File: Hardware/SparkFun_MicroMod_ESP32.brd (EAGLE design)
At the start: 22 x 22 mm, 53 parts, among them J1 MICROMOD-2222, Q2 MBT3904DW1T1, U1 W25QXX128MBIT-6X5, U2 ESP3212, U4 CP2102N, Y1 40MHZ, Y2 32.768kHz

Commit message: updated Prod_IDs
Added missing PROD_IDs
Added Logos to sch
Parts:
- C18: value 100PF -> 100pF
- LOGO2: value (none) -> SFE_LOGO_NAME_FLAME.1_INCH
- LOGO3: value (none) -> OSHW-LOGOS
- R4: value 47.5k -> 33k
- renumbered U$5 to LOGO2, U$8 to LOGO3
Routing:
- net GND: vias 43 -> 46

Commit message: Update SparkFun_MicroMod_ESP32.brd
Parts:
- moved L2 0.25 mm to (1.40, 13.8)
- moved L1 0.25 mm to (2.81, 12.8)
- moved C10 0.13 mm to (1.40, 11.8)
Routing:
- net N$6: track 1.83 -> 2.44 mm
- net GND: vias 46 -> 45
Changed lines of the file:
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@@
 <?xml version="1.0" encoding="utf-8"?>
 <!DOCTYPE eagle SYSTEM "eagle.dtd">
-<eagle version="9.4.1">
+<eagle version="9.6.0">
 <drawing>
 <settings>
@@
 <setting verticaltext="up"/>
 </settings>
-<grid distance="0.05" unitdist="inch" unit="mm" style="lines" multiple="1" display="yes" altdistance="0.005" altunitdist="inch" altunit="inch"/>
+<grid distance="0.05" unitdist="inch" unit="inch" style="lines" multiple="1" display="yes" altdistance="0.005" altunitdist="inch" altunit="inch"/>
 <layers>
 <layer number="1" name="Top" color="4" fill="1" visible="yes" active="yes"/>
@@
 <layer number="38" name="bTest" color="7" fill="1" visible="no" active="yes"/>
 <layer number="39" name="tKeepout" color="4" fill="11" visible="yes" active="yes"/>
-<layer number="40" name="bKeepout" color="1" fill="11" visible="yes" active="yes"/>
+<layer number="40" name="bKeepout" color="1" fill="11" visible="no" active="yes"/>
 <layer number="41" name="tRestrict" color="4" fill="10" visible="no" active="yes"/>
 <layer number="42" name="bRestrict" color="1" fill="10" visible="no" active="yes"/>
 <layer number="43" name="vRestrict" color="2" fill="10" visible="no" active="yes"/>
 <layer number="44" name="Drills" color="7" fill="1" visible="no" active="yes"/>
-<layer number="45" name="Holes" color="7" fill="1" visible="no" active="yes"/>
+<layer number="45" name="Holes" color="7" fill="1" visible="yes" active="yes"/>
 <layer number="46" name="Milling" color="3" fill="1" visible="no" active="yes"/>
 <layer number="47" name="Measures" color="7" fill="1" visible="no" active="yes"/>
@@
 <layer number="50" name="dxf" color="7" fill="1" visible="no" active="yes"/>
 <layer number="51" name="tDocu" color="6" fill="1" visible="yes" active="yes"/>
-<layer number="52" name="bDocu" color="7" fill="1" visible="yes" active="yes"/>
+<layer number="52" name="bDocu" color="7" fill="1" visible="no" active="yes"/>
 <layer number="91" name="Nets" color="2" fill="1" visible="no" active="no"/>
 <layer number="92" name="Busses" color="1" fill="1" visible="no" active="no"/>
@@
 <layer number="95" name="Names" color="7" fill="1" visible="no" active="no"/>
 <layer number="96" name="Values" color="7" fill="1" visible="no" active="no"/>
-<layer number="2" name="Horz/PWR" color="16" fill="1" visible="yes" active="yes"/>
+<layer number="2" name="Horz/PWR" color="16" fill="1" visible="no" active="yes"/>
 <layer number="3" name="Route3" color="17" fill="1" visible="no" active="no"/>
 <layer number="4" name="Route4" color="18" fill="1" visible="no" active="no"/>
@@
 <layer number="13" name="Route13" color="21" fill="1" visible="no" active="no"/>
 <layer number="14" name="Route14" color="22" fill="1" visible="no" active="no"/>
-<layer number="15" name="VIRT/GND" color="23" fill="1" visible="yes" active="yes"/>
+<layer number="15" name="VIRT/GND" color="23" fill="1" visible="no" active="yes"/>
 <layer number="53" name="tGND_GNDA" color="7" fill="9" visible="no" active="no"/>
 <layer number="54" name="bGND_GNDA" color="1" fill="9" visible="no" active="no"/>
@@
 <attribute name="VALUE" x="7.781" y="11.137" size="0.762" layer="28" rot="MR90" align="center"/>
 </element>
-<element name="L1" library="SparkFun-Coils" package="0402-TIGHT" value="2.7nH" x="2.812" y="13.08" smashed="yes">
-<attribute name="NAME" x="2.812" y="13.642" size="0.6096" layer="25" font="vector" ratio="20" align="bottom-center"/>
-<attribute name="PROD_ID" value="NDUC-14236" x="2.812" y="13.08" size="1.778" layer="27" font="vector" ratio="15" display="off"/>
-<attribute name="VALUE" x="2.812" y="12.518" size="0.6096" layer="27" font="vector" ratio="20" align="top-center"/>
-</element>
-<element name="L2" library="SparkFun-Coils" package="0402-TIGHT" value="2nH" x="1.397" y="13.578" smashed="yes" rot="R270">
-<attribute name="NAME" x="1.959" y="13.578" size="0.6096" layer="25" font="vector" ratio="20" rot="R270" align="bottom-center"/>
-<attribute name="PROD_ID" value="NDUC-14238" x="1.397" y="13.578" size="1.778" layer="27" font="vector" ratio="15" rot="R270" display="off"/>
-<attribute name="VALUE" x="0.835" y="13.578" size="0.6096" layer="27" font="vector" ratio="20" rot="R270" align="top-center"/>
-</element>
-<element name="C10" library="SparkFun-Capacitors" package="0402-TIGHT" value="0.5pF" x="1.397" y="11.667" smashed="yes" rot="R270">
-<attribute name="NAME" x="1.959" y="11.667" size="0.6096" layer="25" font="vector" ratio="20" rot="R270" align="bottom-center"/>
-<attribute name="PROD_ID" value="CAP-14362" x="1.397" y="11.667" size="1.778" layer="27" font="vector" ratio="15" rot="R270" display="off"/>
-<attribute name="VALUE" x="0.835" y="11.667" size="0.6096" layer="27" font="vector" ratio="20" rot="R270" align="top-center"/>
+<element name="L1" library="SparkFun-Coils" package="0402-TIGHT" value="2.7nH" x="2.812" y="12.826" smashed="yes">
+<attribute name="NAME" x="2.812" y="13.388" size="0.6096" layer="25" font="vector" ratio="20" align="bottom-center"/>
+<attribute name="PROD_ID" value="NDUC-14236" x="2.812" y="12.826" size="1.778" layer="27" font="vector" ratio="15" display="off"/>
+<attribute name="VALUE" x="2.812" y="12.264" size="0.6096" layer="27" font="vector" ratio="20" align="top-center"/>
+</element>
+<element name="L2" library="SparkFun-Coils" package="0402-TIGHT" value="2nH" x="1.397" y="13.832" smashed="yes" rot="R270">
+<attribute name="NAME" x="1.959" y="13.832" size="0.6096" layer="25" font="vector" ratio="20" rot="R270" align="bottom-center"/>
+<attribute name="PROD_ID" value="NDUC-14238" x="1.397" y="13.832" size="1.778" layer="27" font="vector" ratio="15" rot="R270" display="off"/>
+<attribute name="VALUE" x="0.835" y="13.832" size="0.6096" layer="27" font="vector" ratio="20" rot="R270" align="top-center"/>
+</element>
+<element name="C10" library="SparkFun-Capacitors" package="0402-TIGHT" value="0.5pF" x="1.397" y="11.794" smashed="yes" rot="R270">
+<attribute name="NAME" x="1.959" y="11.794" size="0.6096" layer="25" font="vector" ratio="20" rot="R270" align="bottom-center"/>
+<attribute name="PROD_ID" value="CAP-14362" x="1.397" y="11.794" size="1.778" layer="27" font="vector" ratio="15" rot="R270" display="off"/>
+<attribute name="VALUE" x="0.835" y="11.794" size="0.6096" layer="27" font="vector" ratio="20" rot="R270" align="top-center"/>
 </element>
 <element name="FD1" library="SparkFun-Aesthetics" package="FIDUCIAL-MICRO" value="FIDUCIALUFIDUCIAL" x="0.614" y="5" smashed="yes"/>
@@
 <via x="5.978" y="13.751" extent="1-16" drill="0.2"/>
 <via x="7.108" y="13.471" extent="1-16" drill="0.2"/>
-<via x="2.818" y="12.391" extent="1-16" drill="0.2"/>
+<via x="2.818" y="12.137" extent="1-16" drill="0.2"/>
 <via x="1.088" y="6.011" extent="1-16" drill="0.2"/>
-<via x="6.378" y="12.551" extent="1-16" drill="0.2"/>
 <wire x1="9.15" y1="17.718" x2="8.93" y2="17.498" width="0.2032" layer="1"/>
 <wire x1="8.93" y1="17.498" x2="7.74" y2="17.498" width="0.2032" layer="1"/>
@@
 <via x="3.988" y="13.741" extent="1-16" drill="0.2"/>
 <via x="5.008" y="13.691" extent="1-16" drill="0.2"/>
-<via x="5.588" y="12.551" extent="1-16" drill="0.2"/>
-<via x="4.768" y="12.541" extent="1-16" drill="0.2"/>
-<via x="3.948" y="12.541" extent="1-16" drill="0.2"/>
+<via x="5.969" y="12.297" extent="1-16" drill="0.2"/>
+<via x="5.022" y="12.287" extent="1-16" drill="0.2"/>
+<via x="4.075" y="12.287" extent="1-16" drill="0.2"/>
 <via x="19.62" y="15.33" extent="1-16" drill="0.2"/>
 <via x="12.972" y="18.357" extent="1-16" drill="0.2"/>
@@
 <contactref element="L2" pad="1"/>
 <contactref element="A1" pad="FEED"/>
-<wire x1="1.397" y1="14.078" x2="1.397" y2="16.08" width="0.2032" layer="1"/>
+<wire x1="1.397" y1="14.332" x2="1.397" y2="16.08" width="0.2032" layer="1"/>
 </signal>
 <signal name="N$6">
@@
 <contactref element="L1" pad="1"/>
 <contactref element="C10" pad="1"/>
-<wire x1="2.312" y1="13.08" x2="2.31" y2="13.078" width="0.2032" layer="1"/>
-<wire x1="2.31" y1="13.078" x2="1.397" y2="13.078" width="0.2032" layer="1"/>
-<wire x1="1.397" y1="12.167" x2="1.397" y2="13.078" width="0.2032" layer="1"/>
+<wire x1="2.312" y1="12.826" x2="1.423" y2="12.826" width="0.2032" layer="1"/>
+<wire x1="1.423" y1="12.826" x2="1.397" y2="12.852" width="0.2032" layer="1"/>
+<wire x1="1.397" y1="13.332" x2="1.397" y2="12.852" width="0.2032" layer="1"/>
+<wire x1="1.397" y1="12.294" x2="1.397" y2="13.332" width="0.2032" layer="1"/>
 </signal>
 <signal name="N$8">
 <contactref element="U2" pad="2"/>
 <contactref element="L1" pad="2"/>
-<wire x1="6.87" y1="12.8" x2="8.05" y2="12.8" width="0.2032" layer="1"/>
-<wire x1="3.312" y1="13.08" x2="6.59" y2="13.08" width="0.2032" layer="1"/>
-<wire x1="6.59" y1="13.08" x2="6.87" y2="12.8" width="0.2032" layer="1"/>
+<wire x1="8.05" y1="12.8" x2="3.455" y2="12.8" width="0.2032" layer="1"/>
+<wire x1="3.455" y1="12.8" x2="3.429" y2="12.826" width="0.2032" layer="1"/>
+<wire x1="3.312" y1="12.826" x2="3.429" y2="12.826" width="0.2032" layer="1"/>
 </signal>
 </signals>

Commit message: Updated design
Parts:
- removed L2: 2nH, SparkFun-Coils:0402-TIGHT
- added C8: (no value), SparkFun-Capacitors:0402-TIGHT
- added TP1, TP2: (no value), SparkFun-Connectors:PAD.03X.03
- A1: device SparkFun-RF:ANT-2.4GHZ-3.2X1.6X1.2MM-REDUCED_KEEPOUT -> SparkFun-RF:ANT-2.4GHZ-8.0X1.0MM
- C10: value 0.5pF -> (none)
- Q2: device esp32-thing-temp:SC70-6 -> SparkFun-DiscreteSemi:SC70-6
- U2: value ESP3212 -> ESP32; device esp32-thing-temp:QFN48-0.4MM -> SparkFun-RF:QFN48-0.4MM
- Y1: value 40MHZ -> 40MHz
- moved C10 5.45 mm to (6.63, 13.3), turned to 90 degrees
- moved LOGO3 4.02 mm to (18.6, 5.92)
- moved L1 2.41 mm to (5.22, 12.8)
- moved C20 2.12 mm to (4.97, 16.7), turned to 90 degrees
- moved C26 2.10 mm to (4.83, 5.84), turned to 180 degrees
- moved LOGO2 2.07 mm to (7.11, 17.3)
- moved C9 2.04 mm to (2.79, 5.84), turned to 0 degrees
- moved C7 1.99 mm to (14.3, 18.0), turned to 0 degrees
- moved U4 1.35 mm to (19.0, 15.9)
- moved U$3 1.35 mm to (19.9, 17.7)
- moved A1 1.30 mm to (1.02, 16.5)
- moved R4 1.27 mm to (20.2, 19.2)
- moved R5 1.27 mm to (18.3, 19.2)
- moved R3 1.24 mm to (20.2, 20.1)
- moved C18 1.20 mm to (7.83, 17.6)
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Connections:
- net 13 renamed 13-SPI_!CS!/SD_DATA3
- net 14 renamed 14-SPI_SCK/SD_CLK
- net 15 renamed 15-SPI_MOSI/SD_CMD
- net 2 renamed 2-SPI_MISO/SD_DATA0
- net 21 renamed 21-SDA
- net 22 renamed 22-SCL
- net 23 renamed 23-D0
- net 27 renamed 27-D1
- net 34 renamed 34-A0
- net 35 renamed 35-A1
- net 39 renamed 39-BATT/3
- net 5 renamed 5-STAT_LED
- net CHIP_PU renamed !RESET
- net FLASH_SCK renamed FLASH_SD_CLK
- net FLASH_SCS renamed FLASH_SD_CMD
- net FLASH_SDI renamed FLASH_SD_DATA1
- net FLASH_SDO renamed FLASH_SD_DATA0
- net FLASH_SHD renamed FLASH_SD_DATA2
- net FLASH_SWP renamed FLASH_SD_DATA3
- removed net 0: J1.11, J1.48, Q2.6, R9.1, U2.23
- removed net 12: J1.46, J1.68, U2.18
- removed net 16: J1.20, J1.54, J1.73, U2.25
- removed net 17: J1.22, J1.56, J1.71, U2.27
- removed net 18: J1.40, U2.35
- removed net 19: J1.16, J1.42, U2.38
- removed net 25: J1.52, J1.55, J1.69, U2.14
- removed net 26: J1.50, J1.53, J1.67, U2.15
- removed net 32K_XN: C26.2, J1.47, J1.63, U2.13, Y2.P$2
- removed net 32K_XP: C9.2, J1.32, J1.65, U2.12, Y2.P$1
- removed net 4: J1.44, J1.66, U2.24
- removed net N$6: C10.1, L1.1, L2.2
- removed net V_RTC: J1.72
- new net 0-!BOOT!/I2C_!INT: J1.11, J1.16, Q2.6, R9.1, U2.23
- new net 12-SD_DATA2/G1: J1.42, J1.68, U2.18
- new net 16-G2/RX1/AUD_IN: J1.19, J1.44, J1.54, U2.25
- new net 17-G3/TX1/AUD_OUT: J1.17, J1.46, J1.56, U2.27
- new net 18-PWM0: J1.32, U2.35
- new net 19-PWM1: J1.47, U2.38
- new net 25-G4/AUD_LRCLK/SCL1: J1.48, J1.52, J1.55, U2.14
- new net 26-G5/AUD_BCLK/SDA1: J1.50, J1.53, J1.73, U2.15
- new net 32-G6/RTC: C9.2, J1.71, U2.12, Y2.P$1
- new net 33-G7/RTC: C26.2, J1.69, U2.13, Y2.P$2
- new net 4-SD_DATA1/G0: J1.40, J1.66, U2.24
- net GND: now also C8.2
- net N$5: now also C8.1, L1.1; no longer L2.1
- net N$8: now also C10.1
- net U0RXD: now also TP1.P$1; no longer J1.19
- net U0TXD: now also TP2.P$1; no longer J1.17
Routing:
- net 17: track 40.9 -> 0.00 mm, vias 4 -> 0
- net 16: track 40.6 -> 0.00 mm, vias 4 -> 0
- net 19: track 29.9 -> 0.00 mm, vias 3 -> 0
- net 0-!BOOT!/I2C_!INT: track 0.00 -> 26.9 mm, vias 0 -> 3
- net 0: track 25.5 -> 0.00 mm, vias 2 -> 0
- net 17-G3/TX1/AUD_OUT: track 0.00 -> 25.5 mm, vias 0 -> 3
- net 32K_XP: track 25.3 -> 0.00 mm, vias 2 -> 0
- net 4: track 24.5 -> 0.00 mm, vias 2 -> 0
- net 19-PWM1: track 0.00 -> 24.0 mm, vias 0 -> 2
- net 26-G5/AUD_BCLK/SDA1: track 0.00 -> 23.0 mm, vias 0 -> 2
- net 4-SD_DATA1/G0: track 0.00 -> 22.6 mm, vias 0 -> 2
- net 26: track 21.0 -> 0.00 mm, vias 2 -> 0
- net 16-G2/RX1/AUD_IN: track 0.00 -> 21.0 mm, vias 0 -> 2
- net 12-SD_DATA2/G1: track 0.00 -> 19.4 mm, vias 0 -> 2
- net 25: track 19.0 -> 0.00 mm, vias 2 -> 0
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- added copper zone on layer 15, net 3.3V
- added copper zone on layer 2, net GND
- removed copper zone on layer 2, net 3.3V
- removed copper zone on layer 15, net GND
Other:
- board text added: "1"
- board text added: "2"
- board text added: "3"
- board text added: "4"
- board text added: "v01"
- board text removed: "v10"

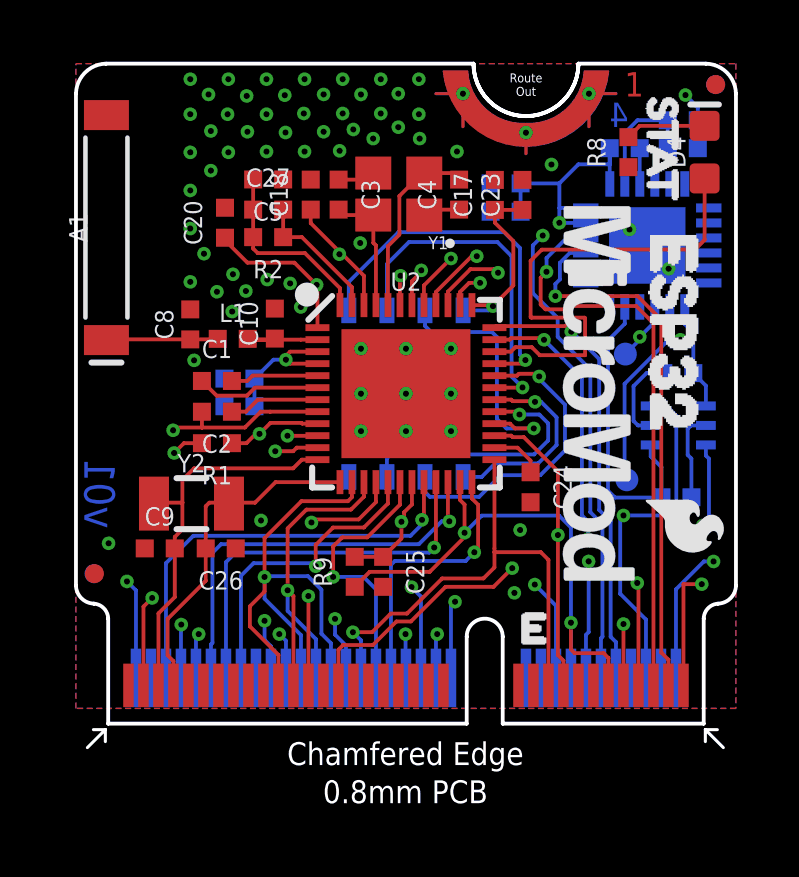
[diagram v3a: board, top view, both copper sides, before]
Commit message: Fixed RF trace Width
- Updated RF trace width to 13mil, added calculation to schematic
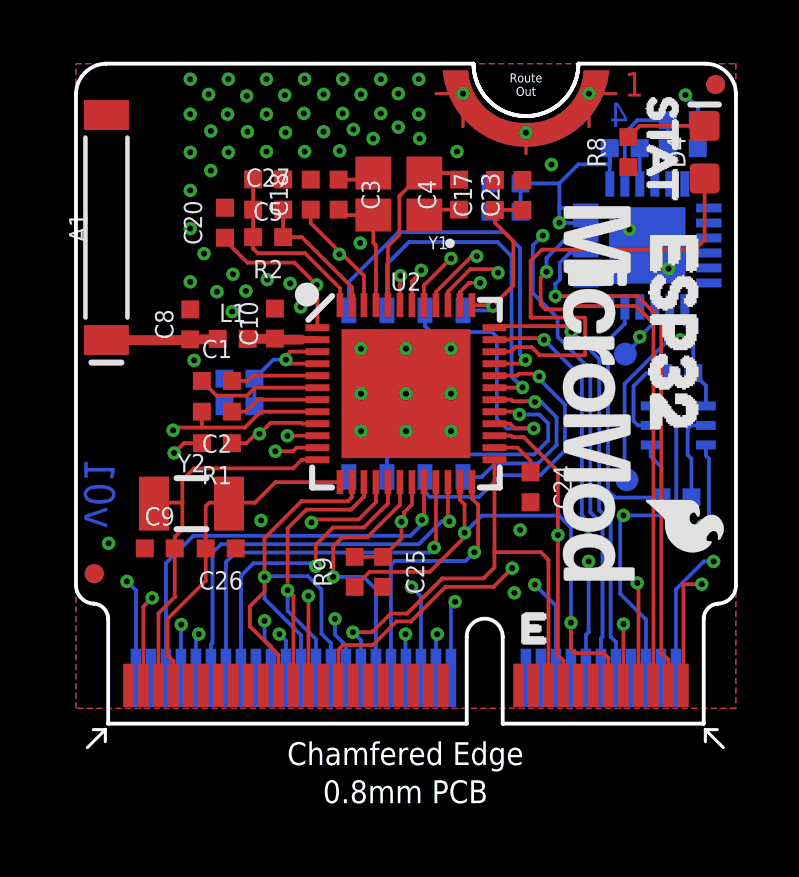
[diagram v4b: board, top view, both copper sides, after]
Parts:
- C10, C8: value (none) -> DNP
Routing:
- net N$8: track 3.07 -> 2.34 mm
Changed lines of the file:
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@@
 <layer number="19" name="Unrouted" color="6" fill="1" visible="yes" active="yes"/>
 <layer number="20" name="Dimension" color="24" fill="1" visible="yes" active="yes"/>
-<layer number="21" name="tPlace" color="16" fill="1" visible="no" active="yes"/>
+<layer number="21" name="tPlace" color="16" fill="1" visible="yes" active="yes"/>
 <layer number="22" name="bPlace" color="14" fill="1" visible="yes" active="yes"/>
 <layer number="23" name="tOrigins" color="15" fill="1" visible="yes" active="yes"/>
@@
 <layer number="28" name="bValues" color="7" fill="1" visible="no" active="yes"/>
 <layer number="29" name="tStop" color="7" fill="3" visible="no" active="yes"/>
-<layer number="30" name="bStop" color="7" fill="6" visible="yes" active="yes"/>
+<layer number="30" name="bStop" color="7" fill="6" visible="no" active="yes"/>
 <layer number="31" name="tCream" color="7" fill="4" visible="no" active="yes"/>
 <layer number="32" name="bCream" color="7" fill="5" visible="no" active="yes"/>
@@
 <layer number="49" name="Reference" color="7" fill="1" visible="no" active="yes"/>
 <layer number="50" name="dxf" color="7" fill="1" visible="no" active="yes"/>
-<layer number="51" name="tDocu" color="6" fill="1" visible="no" active="yes"/>
+<layer number="51" name="tDocu" color="6" fill="1" visible="yes" active="yes"/>
 <layer number="52" name="bDocu" color="7" fill="1" visible="no" active="yes"/>
 <layer number="91" name="Nets" color="2" fill="1" visible="no" active="no"/>
@@
 <layer number="95" name="Names" color="7" fill="1" visible="no" active="no"/>
 <layer number="96" name="Values" color="7" fill="1" visible="no" active="no"/>
-<layer number="2" name="GND" color="16" fill="1" visible="yes" active="yes"/>
+<layer number="2" name="GND" color="16" fill="1" visible="no" active="yes"/>
 <layer number="3" name="Route3" color="17" fill="1" visible="no" active="no"/>
 <layer number="4" name="Route4" color="18" fill="1" visible="no" active="no"/>
@@
 <layer number="13" name="Route13" color="21" fill="1" visible="no" active="no"/>
 <layer number="14" name="Route14" color="22" fill="1" visible="no" active="no"/>
-<layer number="15" name="PWR" color="14" fill="1" visible="yes" active="yes"/>
+<layer number="15" name="PWR" color="14" fill="1" visible="no" active="yes"/>
 <layer number="53" name="tGND_GNDA" color="7" fill="9" visible="no" active="no"/>
 <layer number="54" name="bGND_GNDA" color="1" fill="9" visible="no" active="no"/>
@@
 <attribute name="VALUE" x="1.651" y="16.5354" size="0.6096" layer="27" font="vector" ratio="20" rot="R90" align="top-center"/>
 </element>
-<element name="C8" library="SparkFun-Capacitors" package="0402-TIGHT" value="" x="3.81" y="13.3096" smashed="yes" rot="R90">
+<element name="C8" library="SparkFun-Capacitors" package="0402-TIGHT" value="DNP" x="3.81" y="13.3096" smashed="yes" rot="R90">
 <attribute name="NAME" x="3.248" y="13.3096" size="0.6096" layer="25" font="vector" ratio="20" rot="R90" align="bottom-center"/>
 <attribute name="VALUE" x="4.372" y="13.3096" size="0.6096" layer="27" font="vector" ratio="20" rot="R90" align="top-center"/>
 </element>
-<element name="C10" library="SparkFun-Capacitors" package="0402-TIGHT" value="" x="6.6294" y="13.335" smashed="yes" rot="R90">
+<element name="C10" library="SparkFun-Capacitors" package="0402-TIGHT" value="DNP" x="6.6294" y="13.335" smashed="yes" rot="R90">
 <attribute name="NAME" x="6.0674" y="13.335" size="0.6096" layer="25" font="vector" ratio="20" rot="R90" align="bottom-center"/>
 <attribute name="VALUE" x="7.1914" y="13.335" size="0.6096" layer="27" font="vector" ratio="20" rot="R90" align="top-center"/>
@@
 <contactref element="L1" pad="1"/>
 <contactref element="C8" pad="1"/>
-<wire x1="4.725" y1="12.826" x2="4.7086" y2="12.8096" width="0.127" layer="1"/>
-<wire x1="4.7086" y1="12.8096" x2="3.81" y2="12.8096" width="0.127" layer="1"/>
-<wire x1="1.016" y1="12.7854" x2="1.0402" y2="12.8096" width="0.127" layer="1"/>
-<wire x1="3.81" y1="12.8096" x2="1.0402" y2="12.8096" width="0.127" layer="1"/>
+<wire x1="4.725" y1="12.826" x2="4.7086" y2="12.8096" width="0.3302" layer="1"/>
+<wire x1="4.7086" y1="12.8096" x2="3.81" y2="12.8096" width="0.3302" layer="1"/>
+<wire x1="1.016" y1="12.7854" x2="3.7858" y2="12.7854" width="0.3302" layer="1"/>
+<wire x1="3.7858" y1="12.7854" x2="3.81" y2="12.8096" width="0.3302" layer="1"/>
 </signal>
 <signal name="N$8">
@@
 <contactref element="L1" pad="2"/>
 <contactref element="C10" pad="1"/>
-<wire x1="8.05" y1="12.8" x2="7.4946" y2="12.8" width="0.127" layer="1"/>
-<wire x1="7.4946" y1="12.8" x2="5.9786" y2="12.8" width="0.127" layer="1"/>
-<wire x1="6.6638" y1="12.8006" x2="6.6294" y2="12.835" width="0.127" layer="1"/>
-<wire x1="5.725" y1="12.826" x2="5.9526" y2="12.826" width="0.127" layer="1"/>
-<wire x1="5.978" y1="12.8006" x2="6.6638" y2="12.8006" width="0.127" layer="1"/>
-<wire x1="5.9526" y1="12.826" x2="5.978" y2="12.8006" width="0.127" layer="1"/>
-<wire x1="5.978" y1="12.8006" x2="5.9786" y2="12.8" width="0.127" layer="1"/>
+<wire x1="8.05" y1="12.8" x2="7.52" y2="12.8" width="0.2286" layer="1"/>
+<wire x1="6.6294" y1="12.835" x2="6.6644" y2="12.8" width="0.3302" layer="1"/>
+<wire x1="6.6644" y1="12.8" x2="7.52" y2="12.8" width="0.3302" layer="1"/>
+<wire x1="6.6294" y1="12.835" x2="6.6204" y2="12.826" width="0.3302" layer="1"/>
+<wire x1="6.6204" y1="12.826" x2="5.725" y2="12.826" width="0.3302" layer="1"/>
 </signal>
 <signal name="4-SD_DATA1/G0">
